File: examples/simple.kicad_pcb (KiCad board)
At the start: 2 copper layers, 72.5 x 50 mm, 75 parts, among them J1 Conn_02x10_Odd_Even, Q1 BC847DW, U1 OPA145ID, U10 DG412xY, U2 SN74LV4053ADR, U3 OPA172ID, U4 OPA145ID, U5 OPA172ID, U6 LM4040DBZ-10, U7 OP07, U8 NE5534, U9 OP07

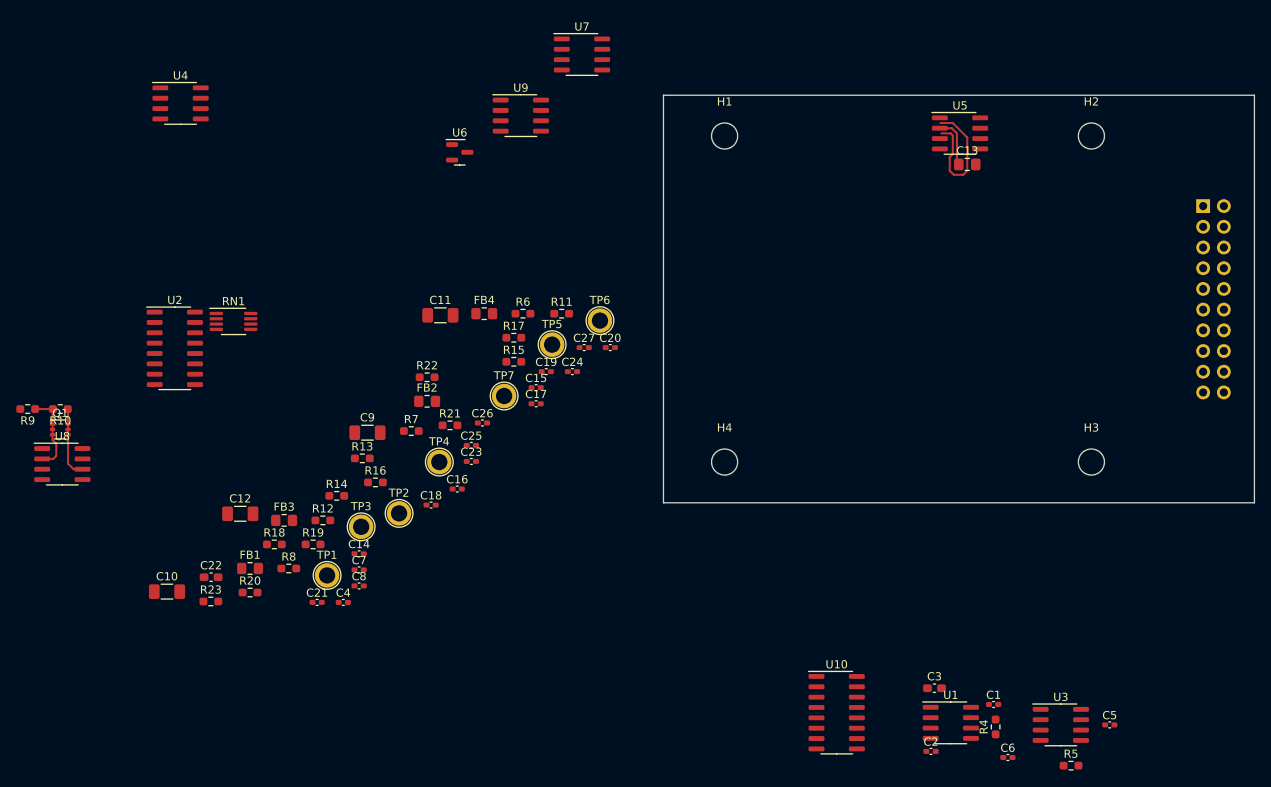
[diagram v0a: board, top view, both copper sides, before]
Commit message: Changed footprints in schematic
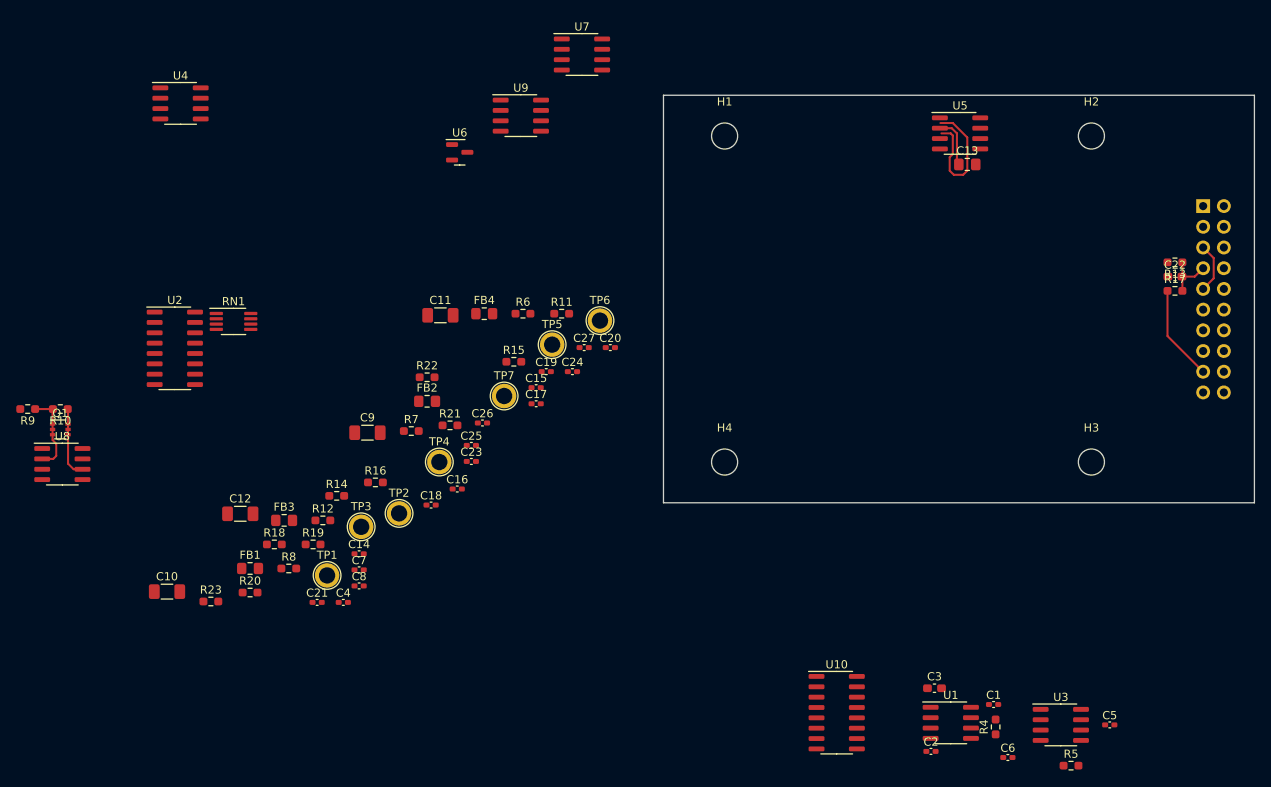
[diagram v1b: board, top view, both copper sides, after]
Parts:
- moved C22 123.9 mm to (185.2, 97.2)
- moved R13 102.6 mm to (185.2, 95.5), turned to 180 degrees
- moved R17 81.3 mm to (185.2, 99.0)
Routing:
- net /DS_OUT: track 0.00 -> 11.7 mm
- net /DS_CMP+: track 0.00 -> 6.57 mm
- net /VREF_CMP-: track 0.00 -> 6.15 mm
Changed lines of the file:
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@@
   )
   (footprint "Resistor_SMD:R_0603_1608Metric_Pad0.98x0.95mm_HandSolder" (layer "F.Cu")
-    (at 85.55 119.55)
+    (at 185.25 95.5 180)
     (descr "Resistor SMD 0603 (1608 Metric), square (rectangular) end terminal, IPC_7351 nominal with elongated pad for handsoldering. (Body size source: IPC-SM-782 page 72, https://www.pcb-3d.com/wordpress/wp-content/uploads/ipc-sm-782a_amendment_1_and_2.pdf), generated with kicad-footprint-generator")
     (tags "resistor handsolder")
@@
     (fp_line (start 0.8 0.4125) (end -0.8 0.4125) (layer "F.Fab") (width 0.1))
     (fp_line (start 0.8 -0.4125) (end 0.8 0.4125) (layer "F.Fab") (width 0.1))
-    (pad "1" smd roundrect (at -0.9125 0) (size 0.975 0.95) (layers "F.Cu" "F.Paste" "F.Mask") (roundrect_rratio 0.25)
+    (pad "1" smd roundrect (at -0.9125 0 180) (size 0.975 0.95) (layers "F.Cu" "F.Paste" "F.Mask") (roundrect_rratio 0.25)
       (net 14 "/DS_CMP+") (pintype "passive"))
-    (pad "2" smd roundrect (at 0.9125 0) (size 0.975 0.95) (layers "F.Cu" "F.Paste" "F.Mask") (roundrect_rratio 0.25)
+    (pad "2" smd roundrect (at 0.9125 0 180) (size 0.975 0.95) (layers "F.Cu" "F.Paste" "F.Mask") (roundrect_rratio 0.25)
       (net 37 "/SLOPE_OUT") (pintype "passive"))
     (model "${KICAD6_3DMODEL_DIR}/Resistor_SMD.3dshapes/R_0603_1608Metric.wrl"
@@
   )
   (footprint "Resistor_SMD:R_0603_1608Metric_Pad0.98x0.95mm_HandSolder" (layer "F.Cu")
-    (at 104.14 104.75)
+    (at 185.25 99)
     (descr "Resistor SMD 0603 (1608 Metric), square (rectangular) end terminal, IPC_7351 nominal with elongated pad for handsoldering. (Body size source: IPC-SM-782 page 72, https://www.pcb-3d.com/wordpress/wp-content/uploads/ipc-sm-782a_amendment_1_and_2.pdf), generated with kicad-footprint-generator")
     (tags "resistor handsolder")
@@
   )
   (footprint "Capacitor_SMD:C_0603_1608Metric_Pad1.08x0.95mm_HandSolder" (layer "F.Cu")
-    (at 67 134.13)
+    (at 185.25 97.25)
     (descr "Capacitor SMD 0603 (1608 Metric), square (rectangular) end terminal, IPC_7351 nominal with elongated pad for handsoldering. (Body size source: IPC-SM-782 page 76, https://www.pcb-3d.com/wordpress/wp-content/uploads/ipc-sm-782a_amendment_1_and_2.pdf), generated with kicad-footprint-generator")
     (tags "capacitor handsolder")
@@
   (segment (start 158.504 83.2575) (end 158.7365 83.49) (width 0.25) (layer "F.Cu") (net 8))
   (segment (start 156.41 79.045) (end 157.869 79.045) (width 0.25) (layer "F.Cu") (net 8))
+  (segment (start 186.1125 97.25) (end 187.68 97.25) (width 0.25) (layer "F.Cu") (net 14))
+  (segment (start 186.1625 97.2) (end 186.1125 97.25) (width 0.25) (layer "F.Cu") (net 14))
+  (segment (start 186.1625 97.3) (end 186.1125 97.25) (width 0.25) (layer "F.Cu") (net 14))
+  (segment (start 186.1625 99) (end 186.1625 97.3) (width 0.25) (layer "F.Cu") (net 14))
+  (segment (start 186.1625 95.5) (end 186.1625 97.2) (width 0.25) (layer "F.Cu") (net 14))
+  (segment (start 187.68 97.25) (end 188.71 96.22) (width 0.25) (layer "F.Cu") (net 14))
+  (segment (start 190 94.97) (end 188.71 93.68) (width 0.25) (layer "F.Cu") (net 22))
+  (segment (start 188.71 98.76) (end 190 97.47) (width 0.25) (layer "F.Cu") (net 22))
+  (segment (start 190 97.47) (end 190 94.97) (width 0.25) (layer "F.Cu") (net 22))
+  (segment (start 184.3375 99) (end 184.3375 104.5475) (width 0.25) (layer "F.Cu") (net 32))
+  (segment (start 184.3375 104.5475) (end 188.71 108.92) (width 0.25) (layer "F.Cu") (net 32))
   (segment (start 47.55 117.3) (end 47.55 116.65) (width 0.25) (layer "F.Cu") (net 36))
   (segment (start 48 119.25) (end 48 117.75) (width 0.25) (layer "F.Cu") (net 36))

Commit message: Layout work
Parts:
- added Q2: MMBT3904, Package_TO_SOT_SMD:SOT-23, F.Cu at (144.0, 68.8)
- added R1: 10K, Resistor_SMD:R_0603_1608Metric_Pad0.98x0.95mm_HandSolder, F.Cu at (148.6, 67.8)
- moved Q1 112.5 mm to (159.8, 99.0)
- moved R10 112.5 mm to (159.8, 96.5)
- moved U8 112.5 mm to (160.0, 103.2)
- moved U4 111.1 mm to (168.1, 112.6)
- moved R9 110.9 mm to (155.2, 108.5), turned to -90 degrees
- moved C14 92.4 mm to (175.5, 111.8)
- moved C21 90.7 mm to (164.5, 104.2), turned to 90 degrees
- moved U2 85.6 mm to (148.1, 107.1), turned to 90 degrees
- moved C8 82.2 mm to (162.8, 108.0), turned to 180 degrees
- moved C7 77.6 mm to (158.5, 108.0), turned to 180 degrees
- moved RN1 75.7 mm to (145.4, 99.9), turned to 90 degrees
- moved FB3 75.2 mm to (149.9, 113.1), turned to -90 degrees
- moved R7 74.8 mm to (166.0, 108.8), turned to 180 degrees
- moved FB1 74.8 mm to (143.9, 113.1), turned to -90 degrees
- moved C15 69.5 mm to (176.3, 114.5)
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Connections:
- RN1 pad 1: unconnected-(RN1-Pad1) -> GNDA
- RN1 pad 2: Net-(U2-Pad4) -> Net-(U2-Pad15)
- RN1 pad 3: Net-(U2-Pad15) -> Net-(U2-Pad4)
- U10 pad 10: GNDS -> /+VREF_Z
- U10 pad 14: unconnected-(U10-Pad14) -> /VIN
- U10 pad 15: unconnected-(U10-Pad15) -> Net-(U10-Pad15)
- U10 pad 16: GND -> /M4
- U10 pad 6: /+VREF_Z -> GNDS
- U10 pad 8: /M2 -> /M3
- U10 pad 9: /M3 -> /M2
- U2 pad 6: GND -> GNDA
- U4 pad 1: unconnected-(U4-Pad1) -> GNDS
- U5 pad 1: unconnected-(U5-Pad1) -> GNDS
- U5 pad 8: unconnected-(U5-Pad8) -> GNDS
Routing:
- net GNDS: track 0.00 -> 76.1 mm
- net /VIN_BUFFERED: track 0.00 -> 35.4 mm
- net GNDA: track 0.00 -> 30.8 mm, vias 0 -> 1
- net /VIN: track 0.00 -> 16.7 mm
- net (no net): track 16.7 -> 0.00 mm
- net +15V: track 0.00 -> 13.6 mm
- net /SUM_NODE: track 6.26 -> 19.4 mm
- net Net-(C3-Pad2): track 0.00 -> 10.3 mm
- net Net-(C3-Pad1): track 0.00 -> 9.93 mm
- net Net-(TP1-Pad1): track 0.00 -> 9.53 mm
- net Net-(R6-Pad1): track 0.00 -> 9.38 mm
- net Net-(U2-Pad4): track 0.00 -> 9.00 mm
- net Net-(FB3-Pad1): track 0.00 -> 7.91 mm
- net -15V: track 0.00 -> 7.82 mm
- net Net-(FB1-Pad1): track 0.00 -> 7.75 mm
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
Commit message: Layout work
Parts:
- moved R23 122.1 mm to (188.0, 121.0), turned to 180 degrees
- moved R18 121.7 mm to (188.0, 85.5)
- moved R19 121.0 mm to (192.0, 85.5), turned to 180 degrees
- moved R20 118.1 mm to (188.0, 115.0), turned to 180 degrees
- moved C4 114.2 mm to (185.0, 85.5), turned to 180 degrees
- moved R12 110.5 mm to (185.2, 91.2), turned to 180 degrees
- moved R16 103.5 mm to (185.2, 89.4)
- moved R8 100.7 mm to (168.0, 91.0)
- moved R22 95.0 mm to (188.0, 119.0), turned to 180 degrees
- moved R21 91.7 mm to (188.0, 117.0), turned to 180 degrees
- moved C10 86.3 mm to (146.0, 118.0)
- moved R15 82.0 mm to (185.2, 95.4)
- moved C16 77.1 mm to (165.2, 87.0), turned to -90 degrees
- moved C12 75.5 mm to (146.0, 122.0)
- moved R14 74.1 mm to (149.2, 92.2)
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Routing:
- net +3V3: track 2.26 -> 110.0 mm, vias 0 -> 2
- net -15V: track 7.82 -> 114.6 mm, vias 0 -> 5
- net /M1: track 0.00 -> 67.8 mm, vias 0 -> 1
- net GND: track 1.80 -> 62.5 mm, vias 0 -> 3
- net /M3: track 0.00 -> 57.7 mm, vias 0 -> 1
- net /M2: track 0.00 -> 56.3 mm, vias 0 -> 1
- net /+VREF_Z: track 0.00 -> 54.3 mm
- net /S1: track 0.00 -> 50.6 mm, vias 0 -> 1
- net /S2: track 0.00 -> 47.9 mm, vias 0 -> 1
- net /S3: track 0.00 -> 44.4 mm, vias 0 -> 1
- net /SLOPE_OUT: track 6.26 -> 38.1 mm
- net /+VREF: track 0.00 -> 25.3 mm
- net +15V: track 13.6 -> 34.4 mm, vias 0 -> 3
- net GNDREF: track 0.00 -> 15.7 mm
- net /-VREF: track 0.00 -> 13.4 mm
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- added copper zone on F.Cu, net +15V
- added copper zone on F.Cu, net -15V
- added copper zone on F.Cu, net /DGND
- added copper zone on F.Cu, net GND
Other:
- copper layers 2 -> 4
- board text added: "+/-10V VREF"

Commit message: Finished layout
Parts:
- removed R21: 0R, Resistor_SMD:R_0603_1608Metric_Pad0.98x0.95mm_HandSolder
- added C28: 100n, Capacitor_SMD:C_0402_1005Metric_Pad0.74x0.62mm_HandSolder, F.Cu at (129.2, 87.0)
- added NT1: NetTie_2, NetTie:NetTie-2_SMD_Pad0.5mm, F.Cu at (154.0, 80.0)
- moved R23 64.1 mm to (136.2, 83.2)
- moved R22 2.00 mm to (188.0, 117.0)
- moved C14 1.00 mm to (172.5, 112.0)
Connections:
- R23 pad 1: /DGND -> GNDREF
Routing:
- net GNDS: track 76.1 -> 148.9 mm
- net -15V: track 114.6 -> 50.7 mm, vias 5 -> 9
- net GNDREF: track 15.7 -> 59.4 mm, vias 0 -> 2
- net GNDA: track 32.1 -> 52.4 mm, vias 1 -> 17
- net GND: track 62.5 -> 73.5 mm
- net +15V: track 34.4 -> 42.1 mm, vias 3 -> 9
- net /M1: track 67.8 -> 65.3 mm
- net +3V3: track 110.0 -> 111.0 mm
- net Net-(Q1-Pad1): track 14.6 -> 15.3 mm
- added copper zone on In1.Cu, net +15V
- added copper zone on In2.Cu, net -15V
- added copper zone on B.Cu, net GNDA
